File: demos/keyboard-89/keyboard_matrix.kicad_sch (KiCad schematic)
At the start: 15 parts, among them K1 TC-6601-5-160G, K10 TC-6601-5-160G, K11 TC-6601-5-160G, K12 TC-6601-5-160G, K13 TC-6601-5-160G, K14 TC-6601-5-160G, K15 TC-6601-5-160G, K2 TC-6601-5-160G, K3 TC-6601-5-160G, K4 TC-6601-5-160G, K5 TC-6601-5-160G, K6 TC-6601-5-160G, K7 TC-6601-5-160G, K8 TC-6601-5-160G, K9 TC-6601-5-160G

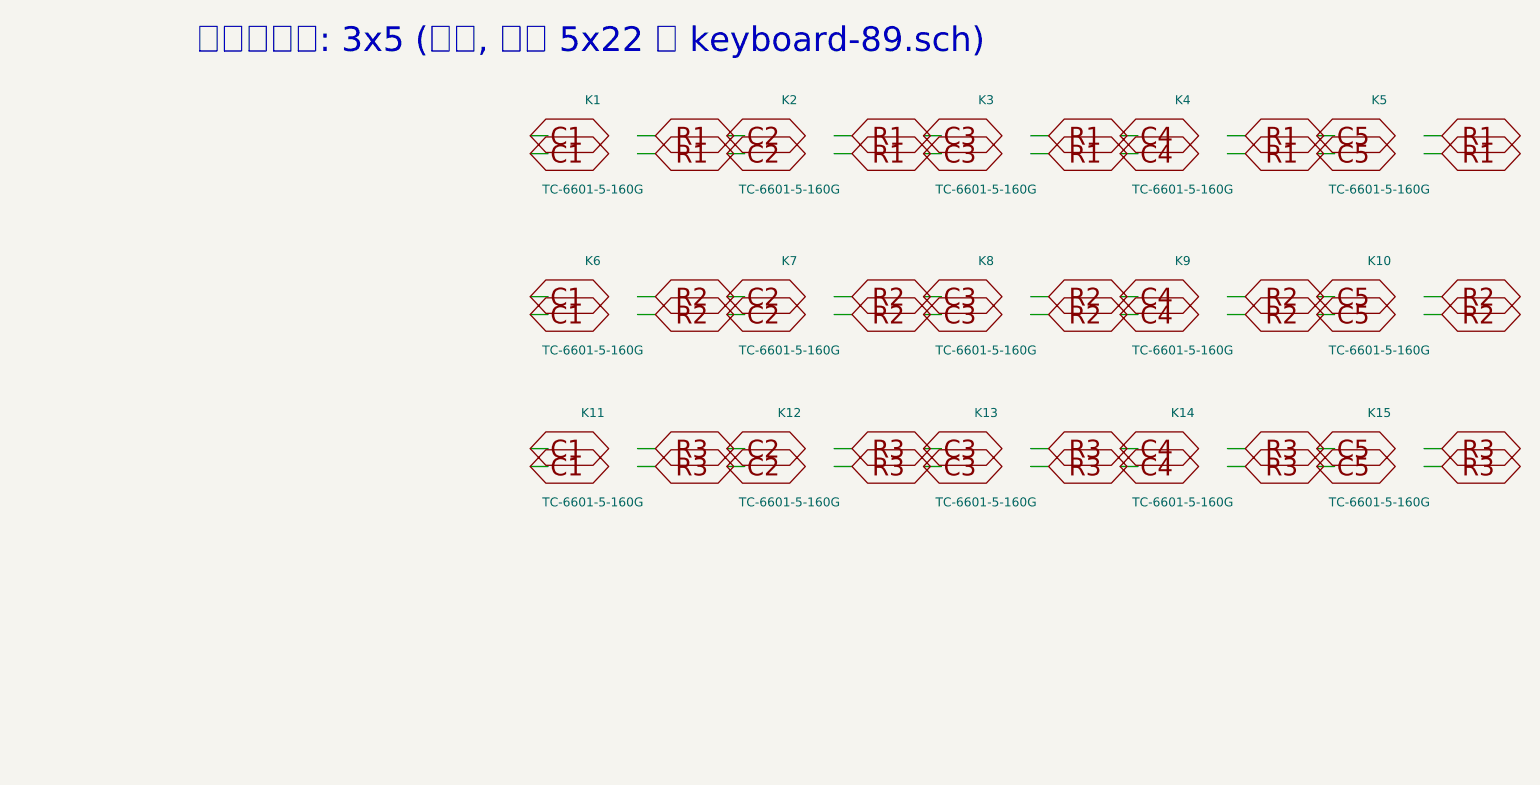
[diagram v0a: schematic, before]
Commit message: fix: update default label height in kicad_sch_add_label function to 1.27mm
feat: add redraw_kb89.py script for redrawing keyboard-89 schematic with new tools
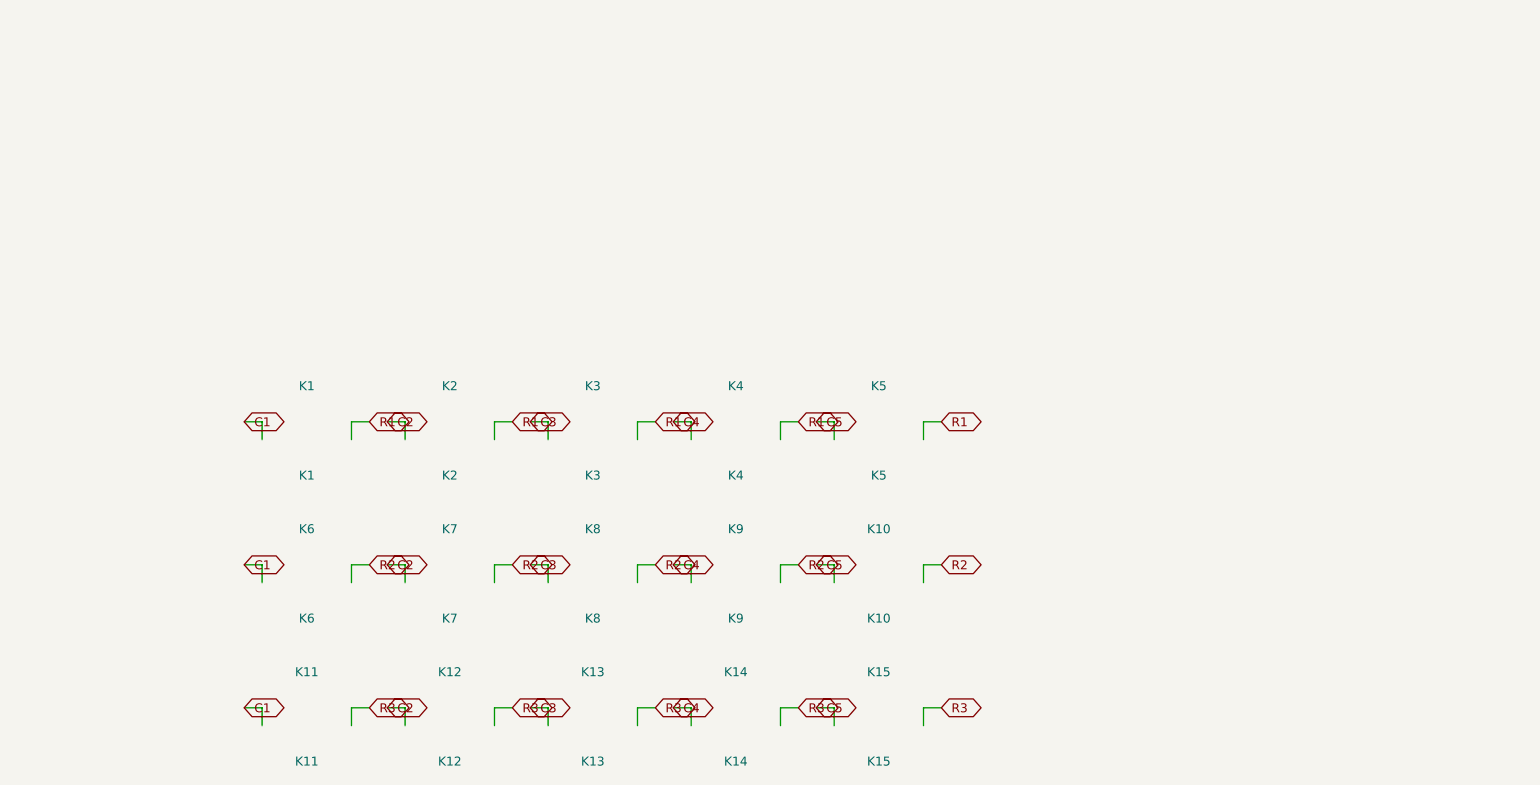
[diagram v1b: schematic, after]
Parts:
- K1: value TC-6601-5-160G -> K1
- K10: value TC-6601-5-160G -> K10
- K11: value TC-6601-5-160G -> K11
- K12: value TC-6601-5-160G -> K12
- K13: value TC-6601-5-160G -> K13
- K14: value TC-6601-5-160G -> K14
- K15: value TC-6601-5-160G -> K15
- K2: value TC-6601-5-160G -> K2
- K3: value TC-6601-5-160G -> K3
- K4: value TC-6601-5-160G -> K4
- K5: value TC-6601-5-160G -> K5
- K6: value TC-6601-5-160G -> K6
- K7: value TC-6601-5-160G -> K7
- K8: value TC-6601-5-160G -> K8
- K9: value TC-6601-5-160G -> K9
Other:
- note removed: "按键矩阵页: 3x5 (示意, 完整 5x22 见 keyboard-89.sch)"

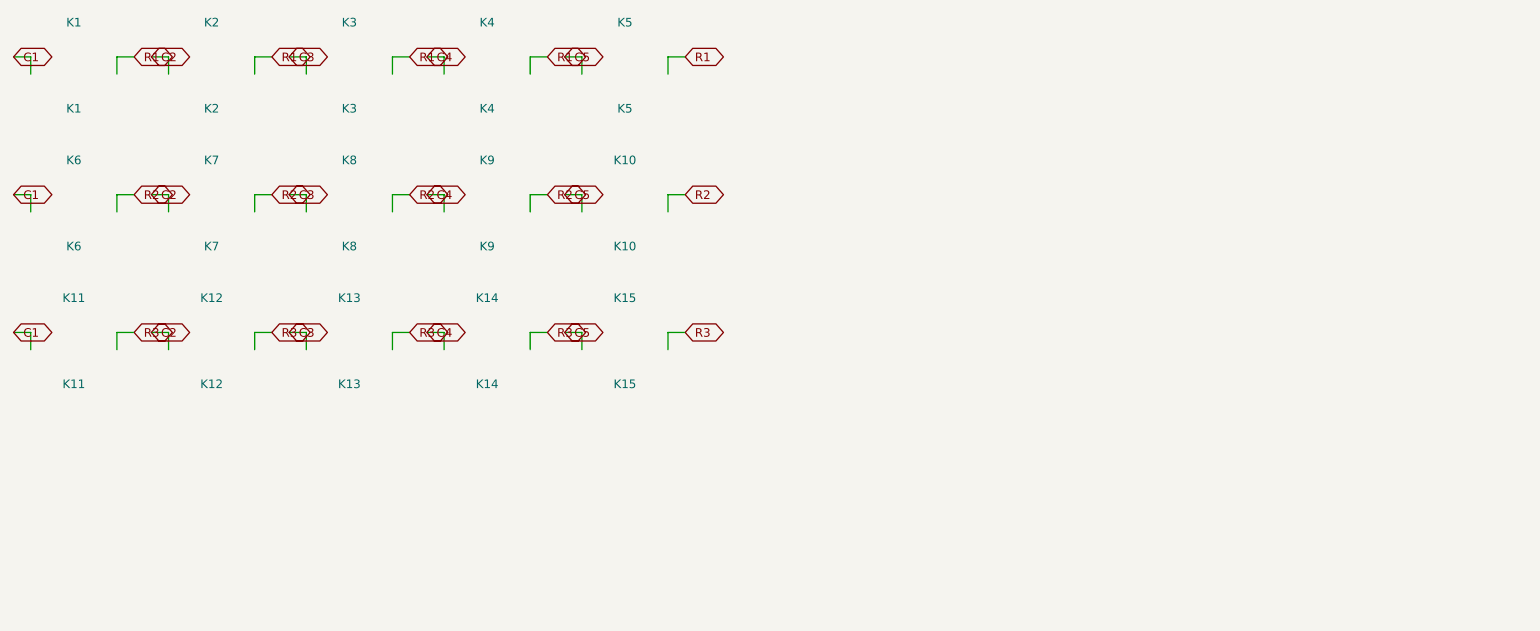
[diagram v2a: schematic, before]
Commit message: feat: add overlap checking and auto repositioning tools
- Introduced a new module for checking and fixing overlaps and out-of-bounds elements in schematic designs.
- Implemented functions to read existing wires and check for overlaps between symbols and labels.
- Enhanced label placement logic to avoid collisions with existing wires.
- Updated the circuit drawing function to utilize the new overlap checking features.
- Modified the redraw tests to accommodate changes in label spacing and positioning.
- Added new tools to the main tools list for easy access.
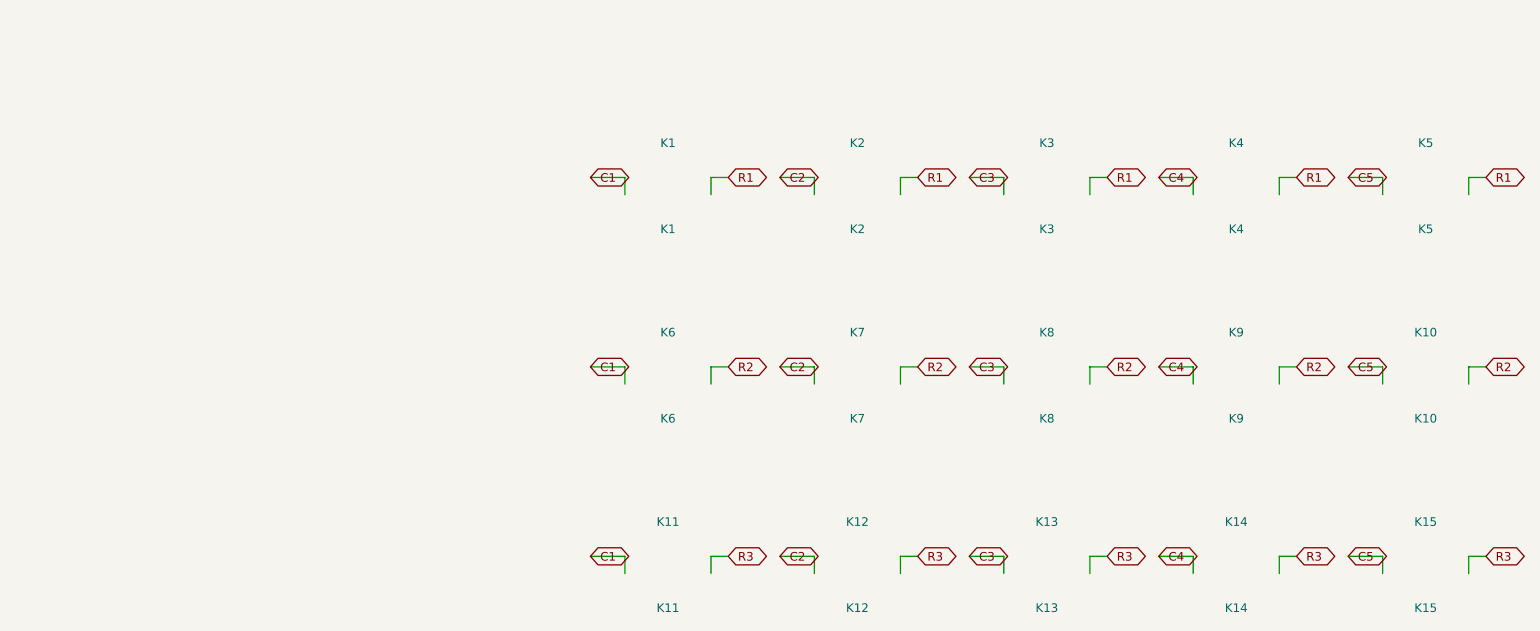
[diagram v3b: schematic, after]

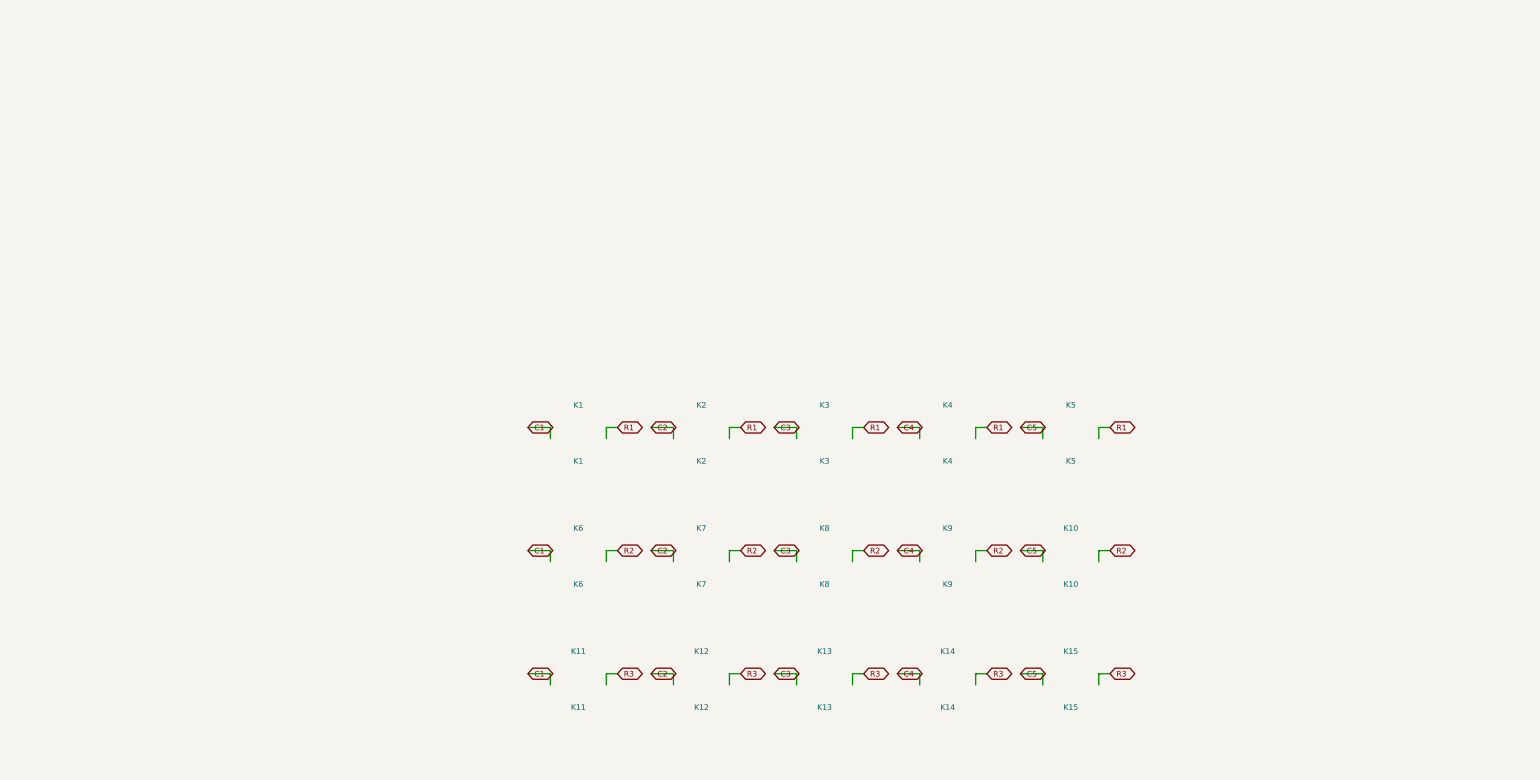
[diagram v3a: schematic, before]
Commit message: Add new footprints for various components in keyboard-89 project
- Added C_0402_1005Metric footprint for 0402 capacitors.
- Added C_0805_2012Metric footprint for 0805 capacitors.
- Added Crystal_YSX321SL footprint for YSX321SL crystals.
- Added D_SOD-123 footprint for SOD-123 diodes.
- Added PinHeader_1x05_P2.54mm_Vertical footprint for 1x05 SWD headers.
- Added QFN-56-1EP_7x7mm_P0.4mm_EP3.2x3.2mm footprint for RP2040 QFN-56 packages.
- Added R_0402_1005Metric footprint for 0402 resistors.
- Added SOIC-8_3.9x4.9mm_P1.27mm footprint for JEDEC MS-012AA SOIC-8 packages.
- Added SOT-89-3 footprint for AMS1117-3.3.
- Added TC-6601-5-160G footprint for 6x6 mm tactile switches.
- Added USB_C_16P_2MD_073 footprint for TYPE-C connectors.
- Created keyboard_controller schematic file for the keyboard-89 project.
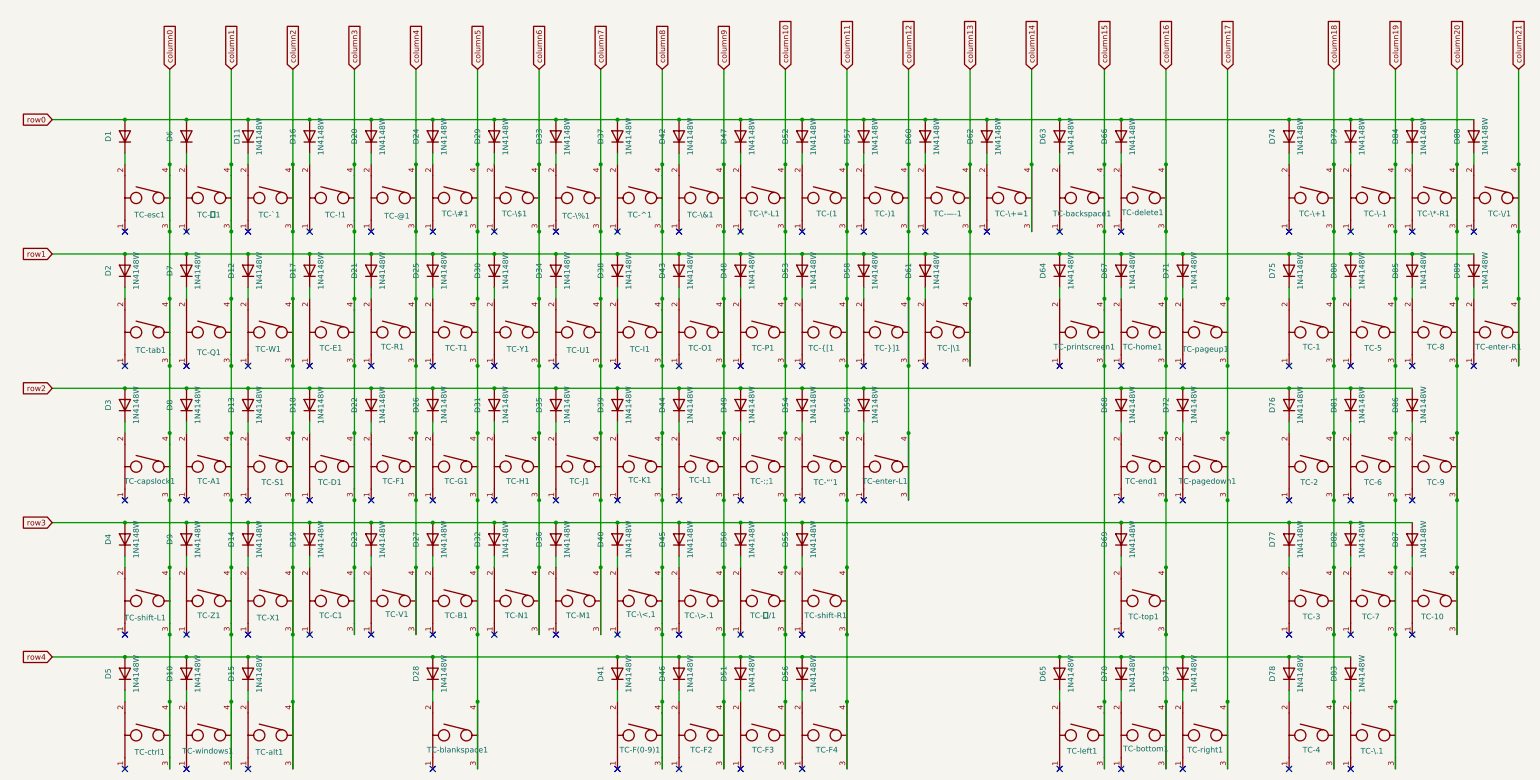
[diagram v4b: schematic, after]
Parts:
- removed K1: K1, symbol keyboard-89_local:TC-6601-5-160G
- removed K10: K10, symbol keyboard-89_local:TC-6601-5-160G
- removed K11: K11, symbol keyboard-89_local:TC-6601-5-160G
- removed K12: K12, symbol keyboard-89_local:TC-6601-5-160G
- removed K13: K13, symbol keyboard-89_local:TC-6601-5-160G
- removed K14: K14, symbol keyboard-89_local:TC-6601-5-160G
- removed K15: K15, symbol keyboard-89_local:TC-6601-5-160G
- removed K2: K2, symbol keyboard-89_local:TC-6601-5-160G
- removed K3: K3, symbol keyboard-89_local:TC-6601-5-160G
- removed K4: K4, symbol keyboard-89_local:TC-6601-5-160G
- removed K5: K5, symbol keyboard-89_local:TC-6601-5-160G
- removed K6: K6, symbol keyboard-89_local:TC-6601-5-160G
- removed K7: K7, symbol keyboard-89_local:TC-6601-5-160G
- removed K8: K8, symbol keyboard-89_local:TC-6601-5-160G
- removed K9: K9, symbol keyboard-89_local:TC-6601-5-160G
- added D1, D10, D11, D12, D13, D14, D15, D16, D17, D18, D19, D2, D20, D21, D22, D23, D24, D25, D26, D27, D28, D29, D3, D30, D31, D32, D33, D34, D35, D36, D37, D38, D39, D4, D40, D41, D42, D43, D44, D45, D46, D47, D48, D49, D5, D50, D51, D52, D53, D54, D55, D56, D57, D58, D59, D6, D60, D61, D62, D63, D64, D65, D66, D67, D68, D69, D7, D70, D71, D72, D73, D74, D75, D76, D77, D78, D79, D8, D80, D81, D82, D83, D84, D85, D86, D87, D88, D89, D9: 1N4148W, keyboard-89_local:D_SOD-123, symbol keyboard-89_local:1N4148W
- added TC-!1, TC-(1, TC-)1, TC-1, TC-10, TC-2, TC-3, TC-4, TC-5, TC-6, TC-7, TC-8, TC-9, TC-:;1, TC-@1, TC-A1, TC-B1, TC-C1, TC-D1, TC-E1, TC-F(0-9)1, TC-F1, TC-F2, TC-F3, TC-F4, TC-G1, TC-H1, TC-I1, TC-J1, TC-K1, TC-L1, TC-M1, TC-N1, TC-O1, TC-P1, TC-Q1, TC-R1, TC-S1, TC-T1, TC-U1, TC-V1, TC-W1, TC-X1, TC-Y1, TC-Z1, TC-\#1, TC-\$1, TC-\%1, TC-\&1, TC-\*-L1, TC-\*-R1, TC-\+1, TC-\+=1, TC-\-1, TC-\.1, TC-\/1, TC-\<,1, TC-\>.1, TC-^1, TC-`1, TC-alt1, TC-backspace1, TC-blankspace1, TC-bottom1, TC-capslock1, TC-ctrl1, TC-delete1, TC-end1, TC-enter-L1, TC-enter-R1, TC-esc1, TC-home1, TC-left1, TC-pagedown1, TC-pageup1, TC-printscreen1, TC-right1, TC-shift-L1, TC-shift-R1, TC-tab1, TC-top1, TC-windows1, TC-{[1, TC-|\1, TC-}]1, TC-—-1, TC-“‘1, TC-？/1, TC-～1: (no value), keyboard-89_local:TC-6601-5-160G, symbol private_lib:TC-6601-5-160G
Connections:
- new net: D33.1 (K), TC-\%1.2
- new net: D63.1 (K), TC-backspace1.2
- new net: D26.1 (K), TC-G1.2
- new net: D7.1 (K), TC-Q1.2
- new net: D87.1 (K), TC-10.2
- new net: D40.1 (K), TC-\<,1.2
- new net: D32.1 (K), TC-N1.2
- new net: D56.1 (K), TC-F4.2
- new net: D6.1 (K), TC-～1.2
- new net: D16.1 (K), TC-!1.2
- new net: D20.1 (K), TC-@1.2
- new net: D41.1 (K), TC-F(0-9)1.2
- new net: D55.1 (K), TC-shift-R1.2
- new net: D59.1 (K), TC-enter-L1.2
- new net: D2.1 (K), TC-tab1.2
- new net: D42.1 (K), TC-\&1.2
- new net: D62.1 (K), TC-\+=1.2
- new net: D13.1 (K), TC-S1.2
- new net: D75.1 (K), TC-1.2
- new net: D22.1 (K), TC-F1.2
- new net: D78.1 (K), TC-4.2
- new net: D44.1 (K), TC-L1.2
- new net: D57.1 (K), TC-)1.2
- new net: D89.1 (K), TC-enter-R1.2
- new net: D35.1 (K), TC-J1.2
- new net: D5.1 (K), TC-ctrl1.2
- new net: D15.1 (K), TC-alt1.2
- new net: D79.1 (K), TC-\-1.2
- new net: D43.1 (K), TC-O1.2
- new net: D86.1 (K), TC-9.2
- new net: D19.1 (K), TC-C1.2
- new net: D77.1 (K), TC-3.2
- new net: D23.1 (K), TC-V1.2
- new net: D85.1 (K), TC-8.2
- new net: D29.1 (K), TC-\$1.2
- new net: D14.1 (K), TC-X1.2
- new net: D30.1 (K), TC-Y1.2
- new net: D58.1 (K), TC-}]1.2
- new net: D66.1 (K), TC-delete1.2
- new net: D34.1 (K), TC-U1.2
- new net: D65.1 (K), TC-left1.2
- new net: D12.1 (K), TC-W1.2
- new net: D84.1 (K), TC-\*-R1.2
- new net: D24.1 (K), TC-\#1.2
- new net: D45.1 (K), TC-\>.1.2
- new net: D60.1 (K), TC-—-1.2
- new net: D1.1 (K), TC-esc1.2
- new net: D73.1 (K), TC-right1.2
- new net: D61.1 (K), TC-|\1.2
- new net: D68.1 (K), TC-end1.2
- new net: D70.1 (K), TC-bottom1.2
- new net: D27.1 (K), TC-B1.2
- new net: D18.1 (K), TC-D1.2
- new net: D46.1 (K), TC-F2.2
- new net: D47.1 (K), TC-\*-L1.2
- new net: D31.1 (K), TC-H1.2
- new net: D88.1 (K), TC-\/1.2
- new net: D80.1 (K), TC-5.2
- new net: D71.1 (K), TC-pageup1.2
- new net: D67.1 (K), TC-home1.2
- new net: D64.1 (K), TC-printscreen1.2
- new net: D25.1 (K), TC-T1.2
- new net: D52.1 (K), TC-(1.2
- new net: D37.1 (K), TC-^1.2
- new net: D69.1 (K), TC-top1.2
- new net: D76.1 (K), TC-2.2
- new net: D49.1 (K), TC-:;1.2
- new net: D17.1 (K), TC-E1.2
- new net: D74.1 (K), TC-\+1.2
- new net: D50.1 (K), TC-？/1.2
- new net: D21.1 (K), TC-R1.2
- new net: D81.1 (K), TC-6.2
- new net: D8.1 (K), TC-A1.2
- new net: D51.1 (K), TC-F3.2
- new net: D38.1 (K), TC-I1.2
- new net: D82.1 (K), TC-7.2
- new net: D10.1 (K), TC-windows1.2
- new net: D39.1 (K), TC-K1.2
- new net: D72.1 (K), TC-pagedown1.2
- new net: D9.1 (K), TC-Z1.2
- new net: D53.1 (K), TC-{[1.2
- new net: D28.1 (K), TC-blankspace1.2
- new net: D11.1 (K), TC-`1.2
- new net: D36.1 (K), TC-M1.2
- new net: D3.1 (K), TC-capslock1.2
- new net: D48.1 (K), TC-P1.2
- new net: D54.1 (K), TC-“‘1.2
- new net: D4.1 (K), TC-shift-L1.2
- new net: D83.1 (K), TC-\.1.2
- new net column0: TC-capslock1.3, TC-capslock1.4, TC-ctrl1.3, TC-ctrl1.4, TC-esc1.3, TC-esc1.4, TC-shift-L1.3, TC-shift-L1.4, TC-tab1.3, TC-tab1.4
- new net column1: TC-A1.3, TC-A1.4, TC-Q1.3, TC-Q1.4, TC-Z1.3, TC-Z1.4, TC-windows1.3, TC-windows1.4, TC-～1.3, TC-～1.4
- new net column10: TC-:;1.3, TC-:;1.4, TC-F3.3, TC-F3.4, TC-P1.3, TC-P1.4, TC-\*-L1.3, TC-\*-L1.4, TC-？/1.3, TC-？/1.4
- new net column11: TC-(1.3, TC-(1.4, TC-F4.3, TC-F4.4, TC-shift-R1.3, TC-shift-R1.4, TC-{[1.3, TC-{[1.4, TC-“‘1.3, TC-“‘1.4
- new net column12: TC-)1.3, TC-)1.4, TC-enter-L1.3, TC-enter-L1.4, TC-}]1.3, TC-}]1.4
- new net column13: TC-|\1.3, TC-|\1.4, TC-—-1.3, TC-—-1.4
- new net column14: TC-\+=1.3, TC-\+=1.4
- new net column15: TC-backspace1.3, TC-backspace1.4, TC-left1.3, TC-left1.4, TC-printscreen1.3, TC-printscreen1.4
- new net column16: TC-bottom1.3, TC-bottom1.4, TC-delete1.3, TC-delete1.4, TC-end1.3, TC-end1.4, TC-home1.3, TC-home1.4, TC-top1.3, TC-top1.4
- new net column17: TC-pagedown1.3, TC-pagedown1.4, TC-pageup1.3, TC-pageup1.4, TC-right1.3, TC-right1.4
- new net column18: TC-1.3, TC-1.4, TC-2.3, TC-2.4, TC-3.3, TC-3.4, TC-4.3, TC-4.4, TC-\+1.3, TC-\+1.4
- new net column19: TC-5.3, TC-5.4, TC-6.3, TC-6.4, TC-7.3, TC-7.4, TC-\-1.3, TC-\-1.4, TC-\.1.3, TC-\.1.4
- new net column2: TC-S1.3, TC-S1.4, TC-W1.3, TC-W1.4, TC-X1.3, TC-X1.4, TC-`1.3, TC-`1.4, TC-alt1.3, TC-alt1.4
- new net column20: TC-10.3, TC-10.4, TC-8.3, TC-8.4, TC-9.3, TC-9.4, TC-\*-R1.3, TC-\*-R1.4
- new net column21: TC-\/1.3, TC-\/1.4, TC-enter-R1.3, TC-enter-R1.4
- new net column3: TC-!1.3, TC-!1.4, TC-C1.3, TC-C1.4, TC-D1.3, TC-D1.4, TC-E1.3, TC-E1.4
- new net column4: TC-@1.3, TC-@1.4, TC-F1.3, TC-F1.4, TC-R1.3, TC-R1.4, TC-V1.3, TC-V1.4
- new net column5: TC-B1.3, TC-B1.4, TC-G1.3, TC-G1.4, TC-T1.3, TC-T1.4, TC-\#1.3, TC-\#1.4, TC-blankspace1.3, TC-blankspace1.4
- new net column6: TC-H1.3, TC-H1.4, TC-N1.3, TC-N1.4, TC-Y1.3, TC-Y1.4, TC-\$1.3, TC-\$1.4
- new net column7: TC-J1.3, TC-J1.4, TC-M1.3, TC-M1.4, TC-U1.3, TC-U1.4, TC-\%1.3, TC-\%1.4
- new net column8: TC-F(0-9)1.3, TC-F(0-9)1.4, TC-I1.3, TC-I1.4, TC-K1.3, TC-K1.4, TC-\<,1.3, TC-\<,1.4, TC-^1.3, TC-^1.4
- new net column9: TC-F2.3, TC-F2.4, TC-L1.3, TC-L1.4, TC-O1.3, TC-O1.4, TC-\&1.3, TC-\&1.4, TC-\>.1.3, TC-\>.1.4
- new net row0: D1.2 (A), D11.2 (A), D16.2 (A), D20.2 (A), D24.2 (A), D29.2 (A), D33.2 (A), D37.2 (A), D42.2 (A), D47.2 (A), D52.2 (A), D57.2 (A), D6.2 (A), D60.2 (A), D62.2 (A), D63.2 (A), D66.2 (A), D74.2 (A), D79.2 (A), D84.2 (A), D88.2 (A)
- new net row1: D12.2 (A), D17.2 (A), D2.2 (A), D21.2 (A), D25.2 (A), D30.2 (A), D34.2 (A), D38.2 (A), D43.2 (A), D48.2 (A), D53.2 (A), D58.2 (A), D61.2 (A), D64.2 (A), D67.2 (A), D7.2 (A), D71.2 (A), D75.2 (A), D80.2 (A), D85.2 (A), D89.2 (A)
- new net row2: D13.2 (A), D18.2 (A), D22.2 (A), D26.2 (A), D3.2 (A), D31.2 (A), D35.2 (A), D39.2 (A), D44.2 (A), D49.2 (A), D54.2 (A), D59.2 (A), D68.2 (A), D72.2 (A), D76.2 (A), D8.2 (A), D81.2 (A), D86.2 (A)
- new net row3: D14.2 (A), D19.2 (A), D23.2 (A), D27.2 (A), D32.2 (A), D36.2 (A), D4.2 (A), D40.2 (A), D45.2 (A), D50.2 (A), D55.2 (A), D69.2 (A), D77.2 (A), D82.2 (A), D87.2 (A), D9.2 (A)
- new net row4: D10.2 (A), D15.2 (A), D28.2 (A), D41.2 (A), D46.2 (A), D5.2 (A), D51.2 (A), D56.2 (A), D65.2 (A), D70.2 (A), D73.2 (A), D78.2 (A), D83.2 (A)
- no-connect marks 0 -> 89
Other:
- company: (none) -> 卢占辉
- title: keyboard_matrix -> 按键原理图
